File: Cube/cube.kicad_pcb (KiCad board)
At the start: 2 copper layers, 59 parts, among them J1 Conn_01x06_Male, J2 Conn_01x03_Male, M1 MNMOS, U1 PIC18F47K40-I_P, U2 TPS56339DDC, U3 AT86RF231-ZU, U4 TPS56339DDC, U5 TPS56339DDC, U6 L3GD20H, U7 Si7007-A20

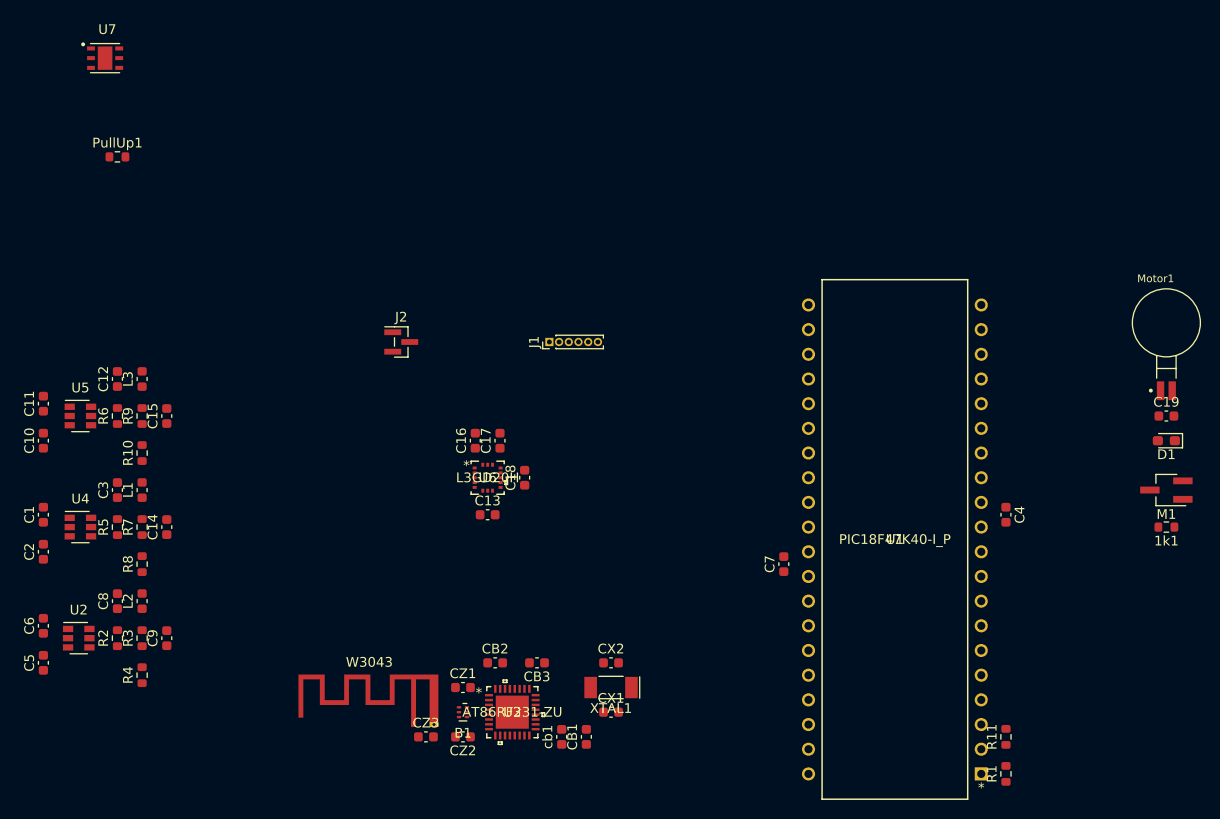
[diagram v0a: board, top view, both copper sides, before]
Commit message: added cube routes
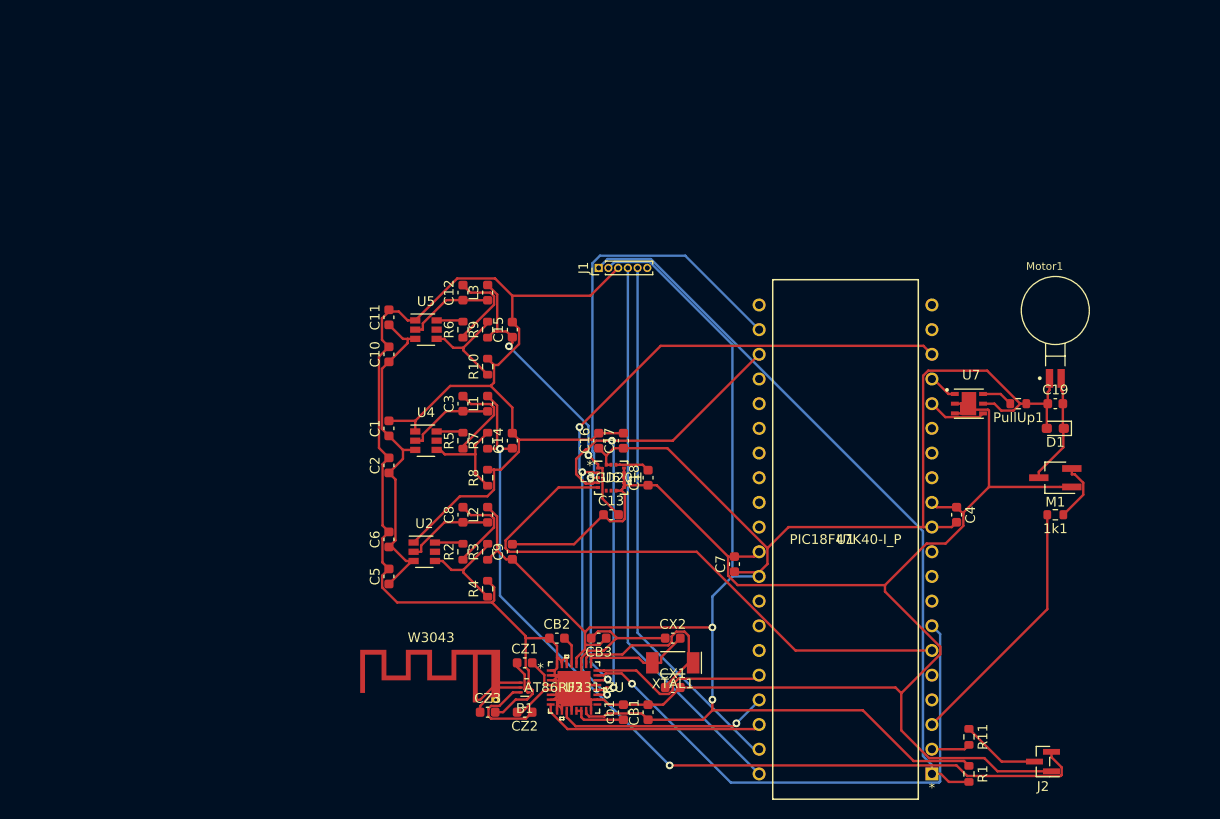
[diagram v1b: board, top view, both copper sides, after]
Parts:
- moved PullUp1 96.1 mm to (158.8, 72.4), turned to 180 degrees
- moved U7 95.7 mm to (153.7, 72.4)
- moved J2 78.9 mm to (161.3, 109.2), turned to 180 degrees
- moved U4 36.7 mm to (97.8, 76.2)
- moved U5 36.7 mm to (97.8, 64.8)
- moved C10 36.7 mm to (94.0, 67.3)
- moved C11 36.7 mm to (94.0, 63.5)
- moved C14 36.7 mm to (106.7, 76.2)
- moved C15 36.7 mm to (106.7, 64.8)
- moved C2 36.7 mm to (94.0, 78.7)
- moved C5 36.7 mm to (94.0, 90.2)
- moved C6 36.7 mm to (94.0, 86.4)
- moved C9 36.7 mm to (106.7, 87.6)
- moved L1 36.7 mm to (104.1, 72.4)
- moved L2 36.7 mm to (104.1, 83.8)
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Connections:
- U7 pad 1: (no net) -> TEMP_OUT
- U7 pad 2: (no net) -> GND
- U7 pad 3: (no net) -> GND
- U7 pad 4: (no net) -> RH_OUT
- U7 pad 5: (no net) -> +3V3
- U7 pad 6: (no net) -> Net-(PullUp1-Pad2)
- U7 pad 7: (no net) -> GND
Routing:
- net GND: track 0.00 -> 357.4 mm
- net +3V3: track 0.00 -> 228.7 mm, vias 0 -> 2
- net +5V: track 0.00 -> 91.9 mm, vias 0 -> 2
- net MCLR: track 0.00 -> 74.9 mm
- net SPI_CLK: track 0.00 -> 71.5 mm, vias 0 -> 3
- net SPI_MOSI: track 0.00 -> 66.3 mm, vias 0 -> 2
- net SPI_CS2: track 0.00 -> 60.8 mm
- net PGD: track 0.00 -> 57.7 mm
- net SPI_CS1: track 0.00 -> 56.4 mm, vias 0 -> 1
- net PGC: track 0.00 -> 55.0 mm
- net SPI_MISO: track 0.00 -> 54.8 mm, vias 0 -> 2
- net VCC: track 0.00 -> 35.4 mm
- net +1V8: track 0.00 -> 31.6 mm, vias 0 -> 2
- net MOTOR_OUT: track 0.00 -> 26.5 mm
- net RESET_ZGB: track 0.00 -> 23.2 mm
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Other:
- net class Default: clearance 0.2 -> 0.05
- rule trace_clearance: 0.2 -> 0.05
